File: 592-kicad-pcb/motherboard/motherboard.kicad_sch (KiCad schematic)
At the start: 2 parts, among them U12 74CBTLV3257, U7 STM32H563ZITx

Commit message: combine hierarchy of all sans power
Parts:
- removed U12: 74CBTLV3257, symbol 74xx:74CBTLV3257
- removed U7: STM32H563ZITx, symbol MCU_ST_STM32H5:STM32H563ZITx
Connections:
- no-connect marks 0 -> 19
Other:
- removed sheet ana_buffers
- removed sheet chip_connection
- removed sheet chip_support_misc
- removed sheet clock_sources
- removed sheet debug_headers
- removed sheet ftdi
- removed sheet memory
- added sheet motherboard_top (motherboard_top.kicad_sch)
- note removed: "DAC1_OUT1"
- note removed: "GPIO_Output (all on this bank)"
- note removed: "I2C1_SCL"
- note removed: "I2C1_SDA"
- note removed: "MASTER TODO: 1) verify caravel support chip configuration 2) correct pull up/down resistors 3) update to new FTDI chip 4) add voltage regulators 5) update nucleo symbol, assign/document pins 6) verify memory interface pinsouts for rocketchip, add connector 7) make connector pinouts match PMOD/JTAG interface on arty"
- note removed: "TIM1_CH1"

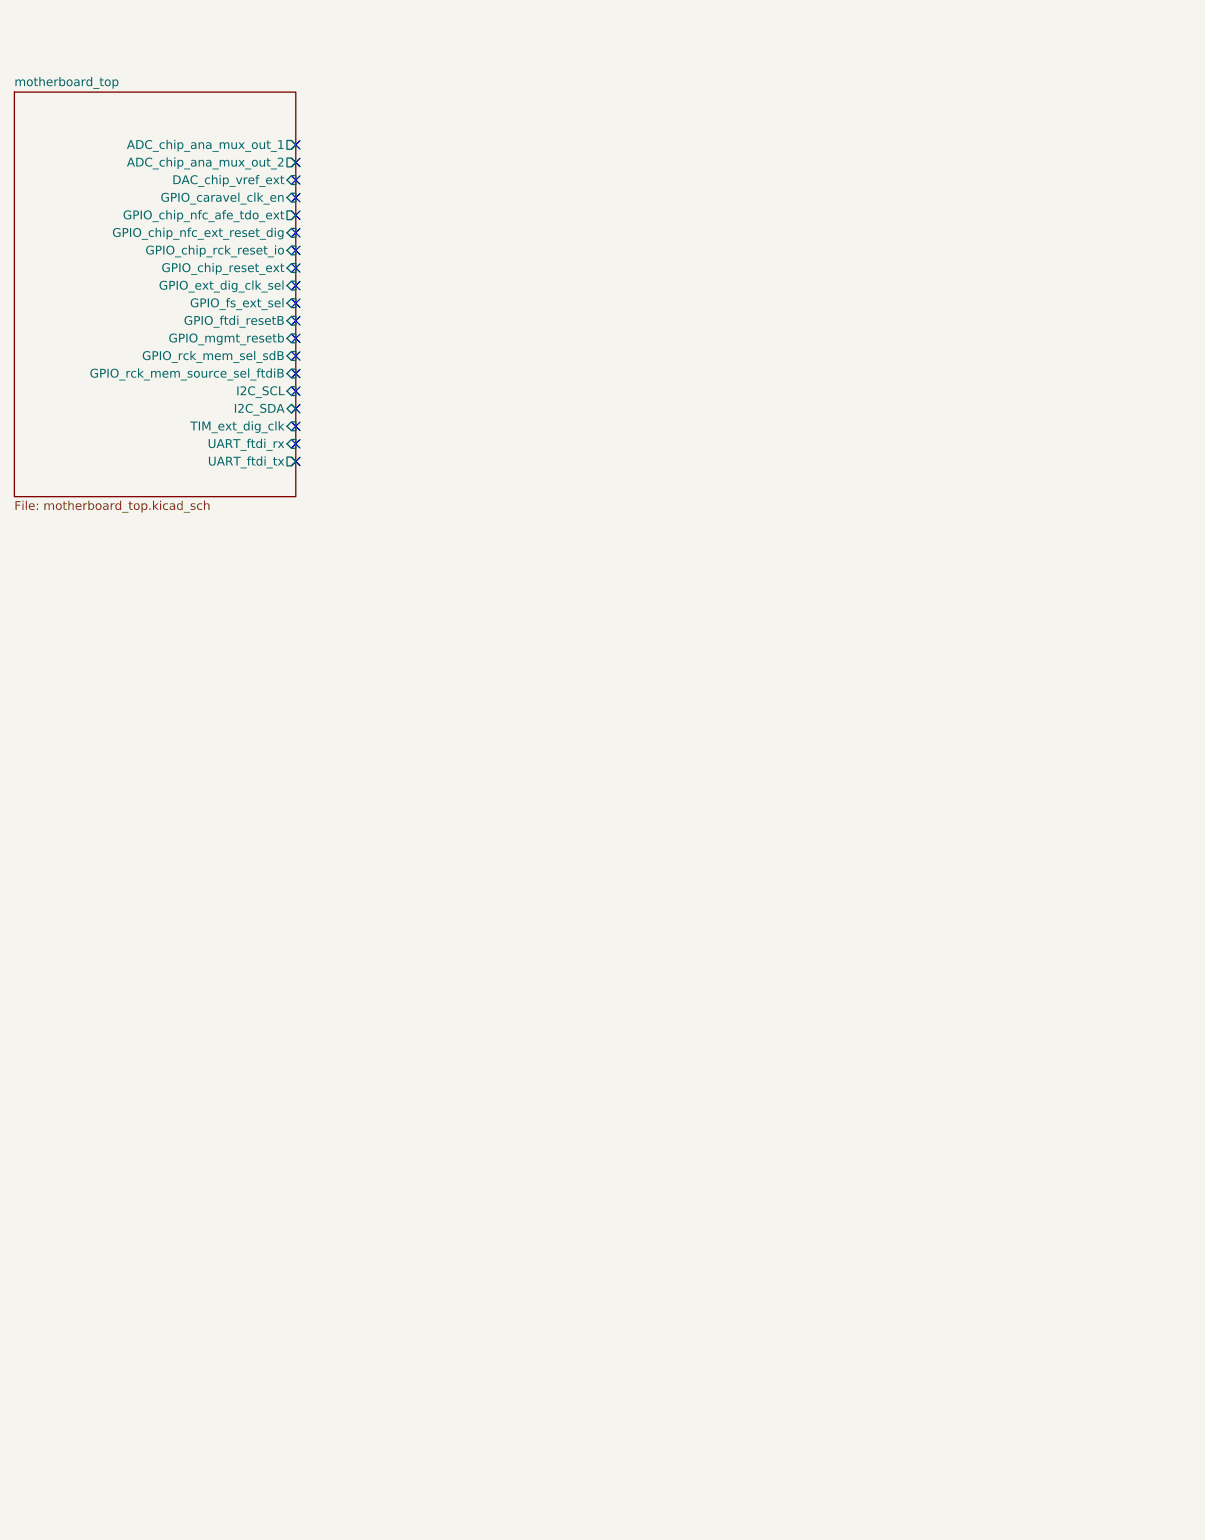
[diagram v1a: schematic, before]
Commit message: partial update to use STM board, updated muxing of FTDI
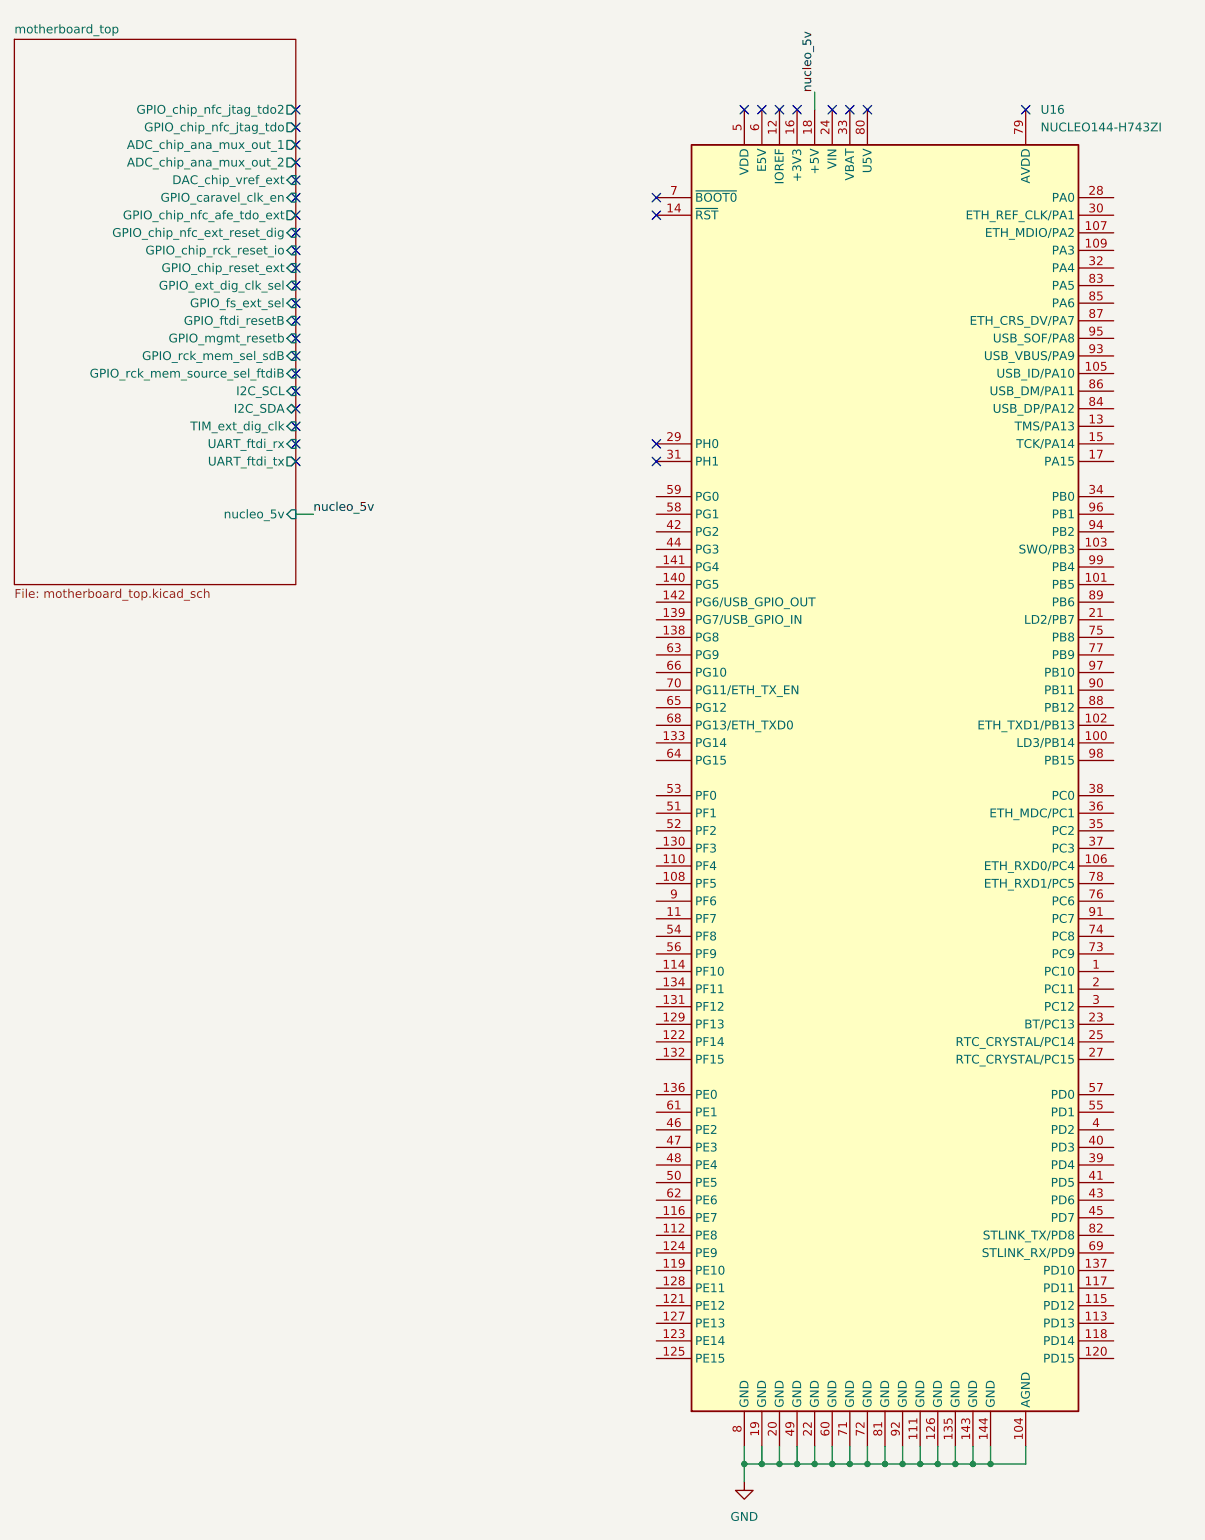
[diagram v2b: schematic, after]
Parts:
- added U16: NUCLEO144-H743ZI, Module:ST_Morpho_Connector_144_STLink, symbol MCU_Module:NUCLEO144-H743ZI
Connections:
- new net GND: U16.104 (AGND), U16.111 (GND), U16.126 (GND), U16.135 (GND), U16.143 (GND), U16.144 (GND), U16.19 (GND), U16.20 (GND), U16.22 (GND), U16.49 (GND), U16.60 (GND), U16.71 (GND), U16.72 (GND), U16.8 (GND), U16.81 (GND), U16.92 (GND)
- new net nucleo_5v: U16.18 (+5V)
- no-connect marks 19 -> 33
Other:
- sheet motherboard_top ports: added GPIO_chip_nfc_jtag_tdo, GPIO_chip_nfc_jtag_tdo2, nucleo_5v; removed none

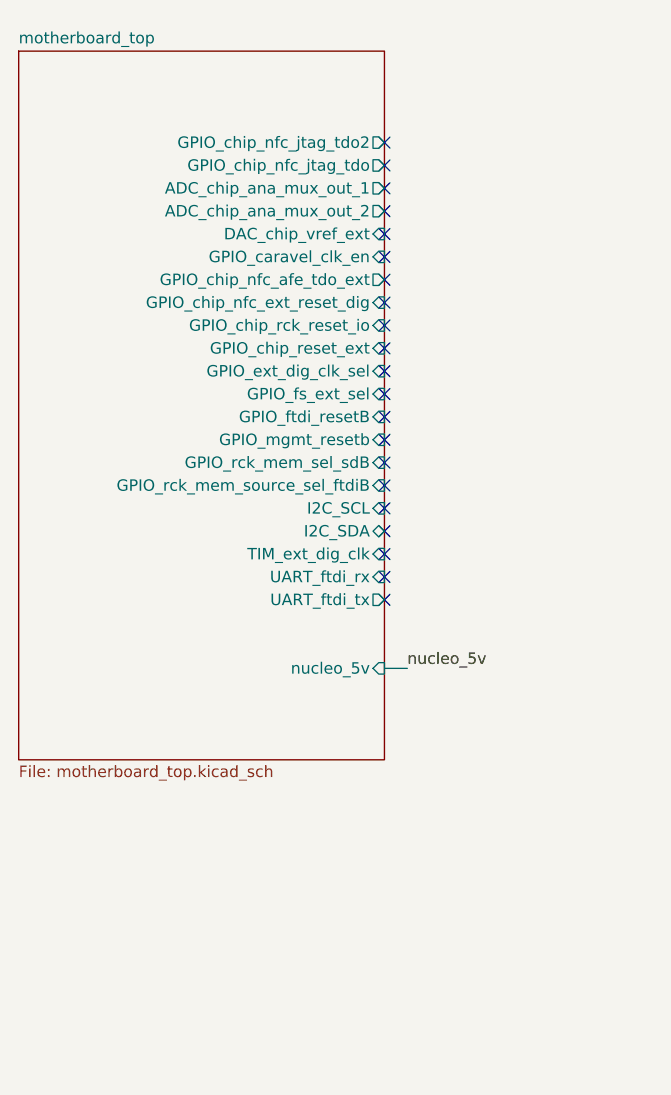
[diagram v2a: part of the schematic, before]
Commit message: update FTDI interfacing
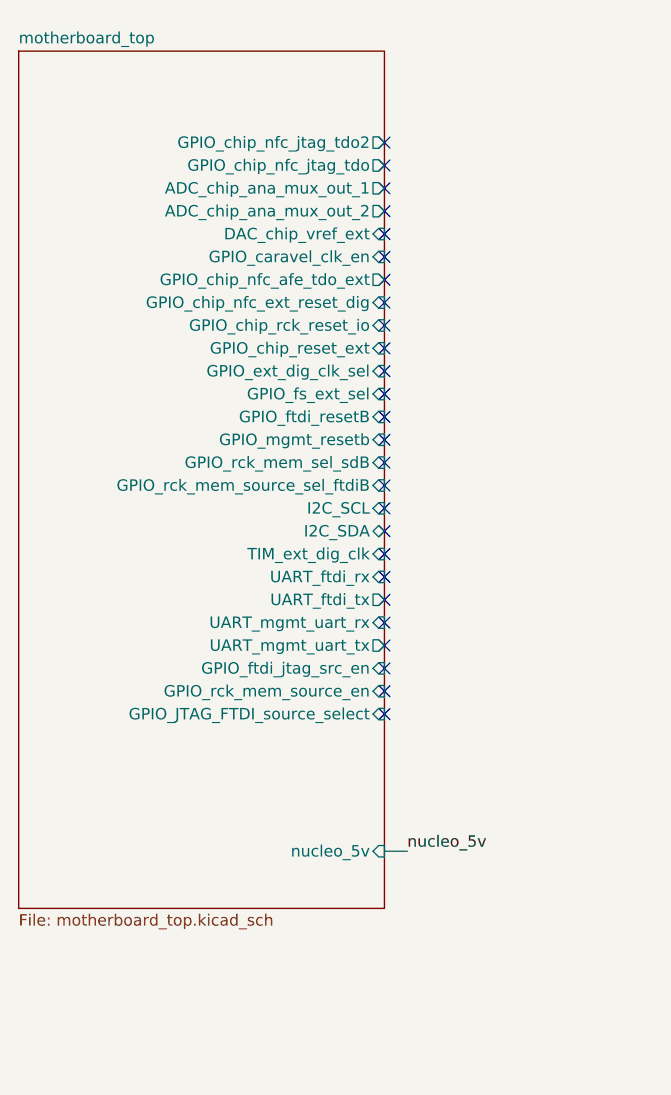
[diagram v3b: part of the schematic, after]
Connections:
- no-connect marks 33 -> 38
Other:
- sheet motherboard_top ports: added GPIO_JTAG_FTDI_source_select, GPIO_ftdi_jtag_src_en, GPIO_rck_mem_source_en, UART_mgmt_uart_rx, UART_mgmt_uart_tx; removed none
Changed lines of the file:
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@@
+	)
+	(no_connect
+		(at 71.12 85.09)
 	)
 	(no_connect
@@
 	)
 	(no_connect
+		(at 71.12 92.71)
+	)
+	(no_connect
 		(at 176.53 29.21)
 	)
@@
 	)
 	(no_connect
+		(at 71.12 82.55)
+	)
+	(no_connect
 		(at 138.43 29.21)
 	)
@@
 	)
 	(no_connect
+		(at 71.12 90.17)
+	)
+	(no_connect
+		(at 71.12 87.63)
+	)
+	(no_connect
 		(at 148.59 29.21)
 	)
@@
 	(wire
 		(pts
-			(xy 71.12 87.63) (xy 73.66 87.63)
+			(xy 71.12 107.95) (xy 73.66 107.95)
 		)
 		(stroke
@@
 	)
 	(label "nucleo_5v"
-		(at 73.66 87.63 0)
+		(at 73.66 107.95 0)
 		(effects
 			(font
@@
 	(sheet
 		(at 30.48 19.05)
-		(size 40.64 78.74)
+		(size 40.64 95.25)
 		(exclude_from_sim no)
 		(in_bom yes)
@@
 		)
 		(property "Sheetfile" "motherboard_top.kicad_sch"
-			(at 30.48 98.3746 0)
+			(at 30.48 114.8846 0)
 			(effects
 				(font
@@
 		)
 		(pin "nucleo_5v" input
-			(at 71.12 87.63 0)
+			(at 71.12 107.95 0)
 			(effects
 				(font
@@
 			(effects
 				(font
+					(size 1.27 1.27)
+				)
+				(justify right)
+			)
+		)
+		(pin "UART_mgmt_uart_rx" input
+			(at 71.12 82.55 0)
+			(effects
+				(font
+					(size 1.27 1.27)
+				)
+				(justify right)
+			)
+		)
+		(pin "UART_mgmt_uart_tx" output
+			(at 71.12 85.09 0)
+			(effects
+				(font
+					(size 1.27 1.27)
+				)
+				(justify right)
+			)
+		)
+		(pin "GPIO_ftdi_jtag_src_en" input
+			(at 71.12 87.63 0)
+			(effects
+				(font
+					(size 1.27 1.27)
+				)
+				(justify right)
+			)
+		)
+		(pin "GPIO_rck_mem_source_en" input
+			(at 71.12 90.17 0)
+			(effects
+				(font
+					(size 1.27 1.27)
+				)
+				(justify right)
+			)
+		)
+		(pin "GPIO_JTAG_FTDI_source_select" input
+			(at 71.12 92.71 0)
+			(effects
+				(font

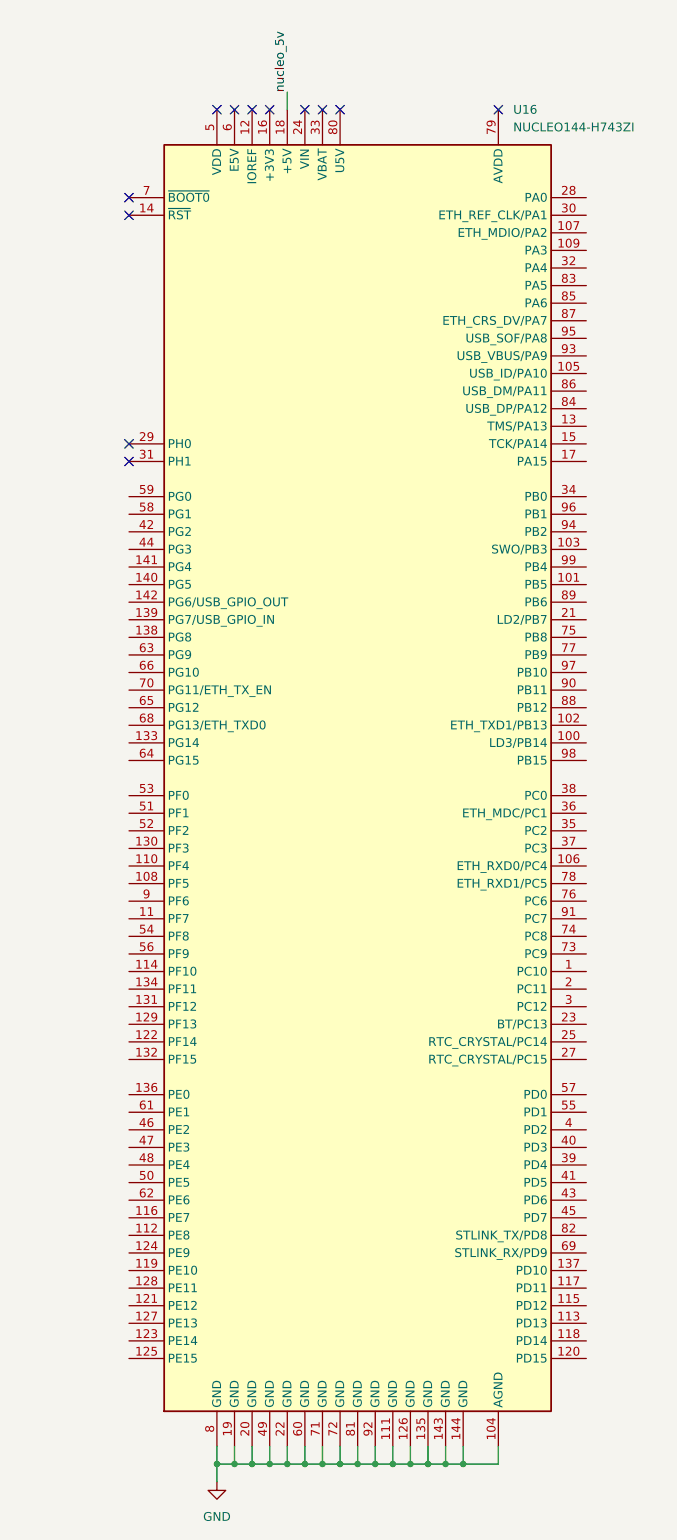
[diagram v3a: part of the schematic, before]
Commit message: add JLC part num for parts, footprints
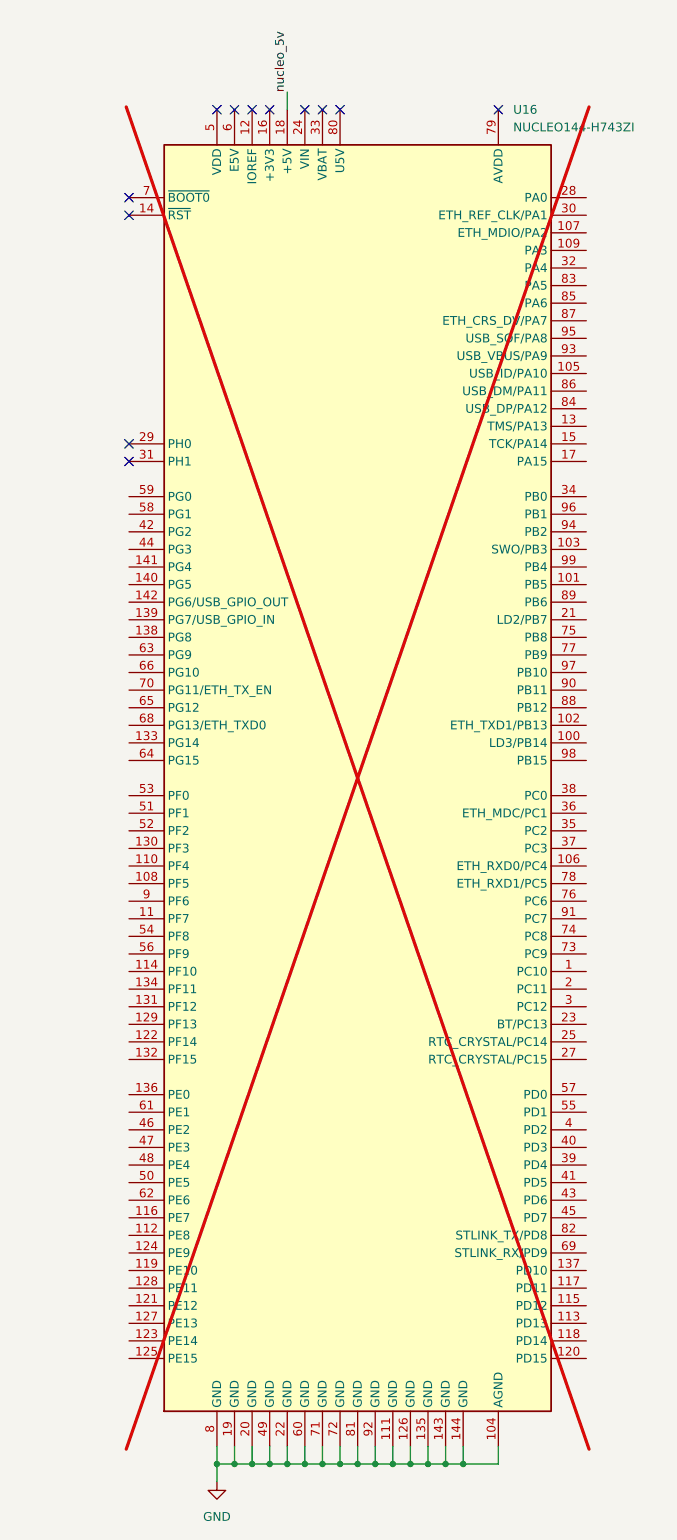
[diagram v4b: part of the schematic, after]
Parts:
- U16: now not fitted
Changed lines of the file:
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@@
 		(in_bom yes)
 		(on_board yes)
-		(dnp no)
+		(dnp yes)
 		(fields_autoplaced yes)
 		(property "Reference" "U16"
